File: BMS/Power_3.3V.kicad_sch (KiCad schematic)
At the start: 6 parts, among them U5 PTPSM863253RDXR

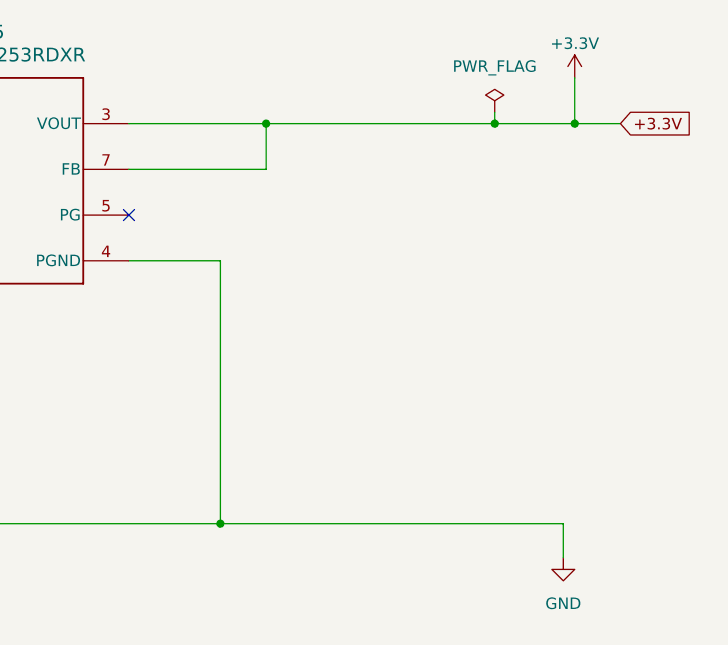
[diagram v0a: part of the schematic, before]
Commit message: Iteracja 1.0 gotowa, teraz sprawdzenie i zmiany kosmetyczne
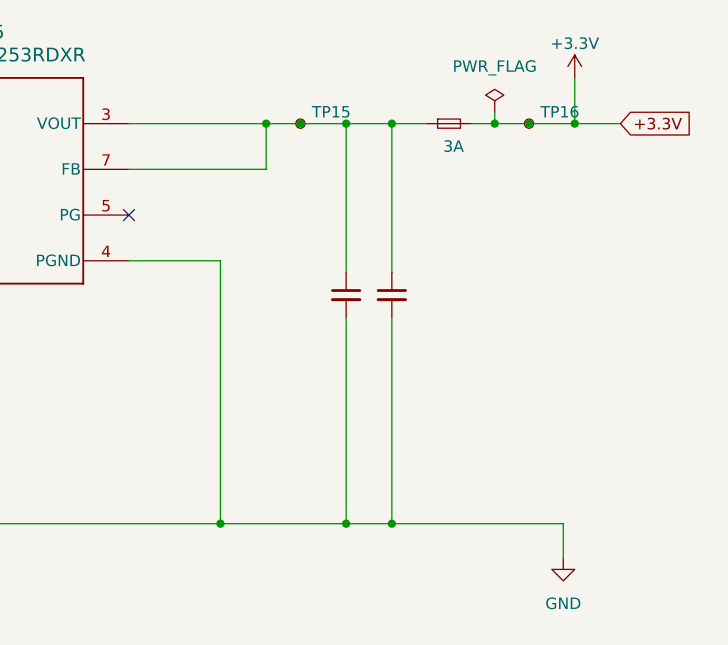
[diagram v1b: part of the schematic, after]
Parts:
- added C137, C138: 1uF, Capacitor_SMD:C_0603_1608Metric_Pad1.08x0.95mm_HandSolder, symbol Device:C_Small
- added F2: 3A, Fuse:Fuse_0603_1608Metric_Pad1.05x0.95mm_HandSolder, symbol Device:Fuse_Small
- added TP15, TP16: TestPoint_Small, TestPoint:TestPoint_Pad_D1.0mm, symbol Connector:TestPoint_Small
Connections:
- net +3.3V: now also F2.2, TP16.1; no longer U5.3 (VOUT), U5.7 (FB)
- net GND: now also C137.2, C138.2
- new net: C137.1, C138.1, F2.1, TP15.1, U5.3 (VOUT), U5.7 (FB)
